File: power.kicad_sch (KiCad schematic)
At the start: 39 parts, among them J11 Conn_01x02_MountingPin, U2 XC6193A103ER-G, U3 TPS631000DRLR, U4 TPS62840DLCR, U5 BQ25185DLHR, U7 LC709203FXE-03MH

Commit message: Update
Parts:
- added R7: 100K, Resistor_SMD:R_0402_1005Metric, symbol Device:R_US
- added R8: 200K, Resistor_SMD:R_0402_1005Metric, symbol Device:R_US
- S6: now not fitted; now left out of the parts list
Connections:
- net +5V_USB: now also R7.2
- net GND: now also R8.2
- new net CHARGER_EN: R7.1, R8.1
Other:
- moved on the sheet: L31, R33

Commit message: Update
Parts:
- S5: now not fitted; now left out of the parts list
- S6: now fitted; now in the parts list
- U7: now left out of the parts list
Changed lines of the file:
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@@
 		(unit 1)
 		(exclude_from_sim no)
-		(in_bom yes)
-		(on_board yes)
-		(dnp no)
+		(in_bom no)
+		(on_board yes)
+		(dnp yes)
 		(property "Reference" "S5"
 			(at 59.182 79.756 0)
@@
 		(unit 1)
 		(exclude_from_sim no)
-		(in_bom yes)
+		(in_bom no)
 		(on_board yes)
 		(dnp no)
@@
 		(unit 1)
 		(exclude_from_sim no)
-		(in_bom no)
-		(on_board yes)
-		(dnp yes)
+		(in_bom yes)
+		(on_board yes)
+		(dnp no)
 		(property "Reference" "S6"
 			(at 98.552 79.756 0)

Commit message: Developer Preview 1
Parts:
- U7: now in the parts list

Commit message: Developer Preview 2
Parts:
- removed D3: RB751S40,115, footprints:RB751S40115, symbol RB751S40_115:RB751S40,115
- removed R7: 100K, Resistor_SMD:R_0402_1005Metric, symbol Device:R_US
- removed R8: 200K, Resistor_SMD:R_0402_1005Metric, symbol Device:R_US
- removed U7: LC709203FXE-03MH, footprints:WLCSP9_1P60X1P76_ONS, symbol 2026-03-20_21-20-11:LC709203FXE-03MH
- added Q21: BC847W, Package_TO_SOT_SMD:SOT-323_SC-70, symbol Transistor_BJT:BC847W
- added R24: 100K, Resistor_SMD:R_0402_1005Metric, symbol Device:R_US
- added U7: MAX17048G+T10, footprints:21-0168E_T822-3_MXM, symbol MAX17048:MAX17048G+T10
- C52: value 1uF -> 22uF
- L31: footprint Inductor_SMD:L_0402_1005Metric -> Inductor_SMD:L_1008_2520Metric
- L41: footprint Inductor_SMD:L_0402_1005Metric -> Inductor_SMD:L_Murata_DFE201610P
- R51: value 1K -> 620
- R52: value 5K -> 18K
- U2: footprint footprints:SON40P150X150X50-9N -> footprints:USP-8B06
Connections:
- net ALARMB is gone; now on net GND: R73.1
- net +3.3V_SYS: no longer R73.2
- net +BATT: now also U7.2 (CELL), U7.3 (VDD)
- net GND: now also Q21.2 (E), U7.1 (CTG), U7.4 (GND), U7.9 (EPAD)
- net SCL: now also R71.1, U7.7 (SCL); no longer R72.1
- net SDA: now also R72.1, U7.8 (SDA); no longer R71.1
- net SW: now also R24.1
- net SW_P: now also Q21.3 (C)
- new net: R73.2, U7.6 (QSTRT)
- new net: Q21.1 (B), R24.2
- no-connect marks 3 -> 2
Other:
- moved on the sheet: R23, S5, S6

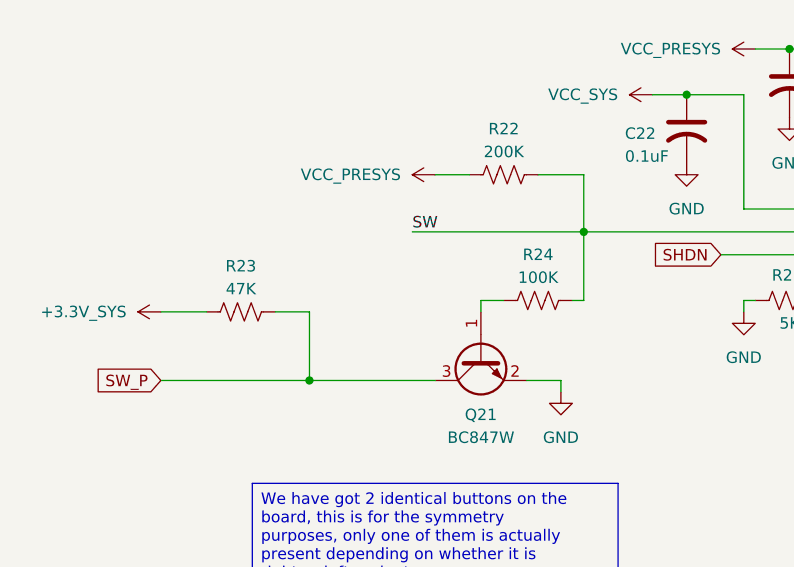
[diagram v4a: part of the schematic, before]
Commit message: Tweak R23 and R24 values
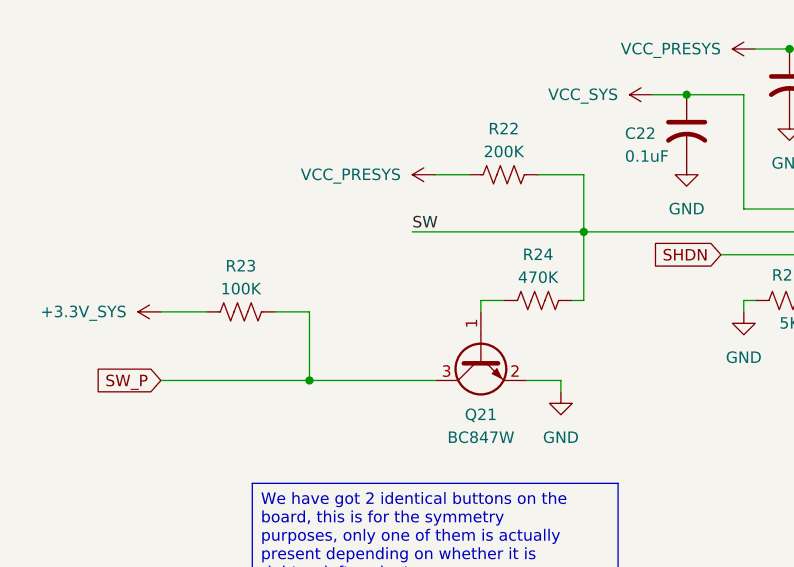
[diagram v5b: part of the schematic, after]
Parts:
- R23: value 47K -> 100K
- R24: value 100K -> 470K
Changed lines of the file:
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@@
 			)
 		)
-		(property "Value" "100K"
+		(property "Value" "470K"
 			(at 69.85 46.99 90)
 			(show_name no)
@@
 			)
 		)
-		(property "Value" "47K"
+		(property "Value" "100K"
 			(at 36.83 48.26 90)
 			(show_name no)
